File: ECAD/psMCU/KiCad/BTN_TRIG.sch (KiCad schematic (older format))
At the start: 9 parts, among them SW4 Btn, U284 SN74LVC1G17DCK, U285 SN74LVC1G32DCK

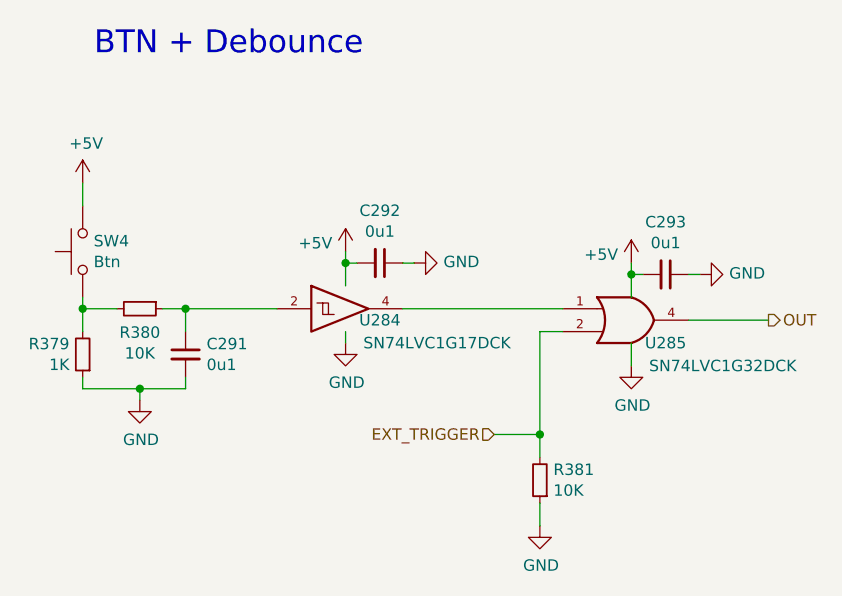
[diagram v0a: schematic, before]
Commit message: Sch: Fixed SYS1 Register
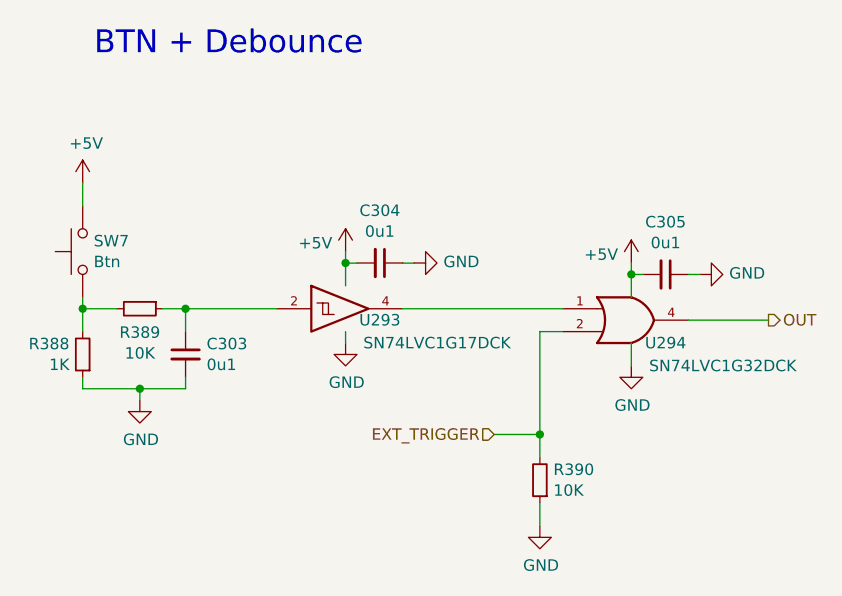
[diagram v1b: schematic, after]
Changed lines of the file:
@@
 $Descr A4 11693 8268
 encoding utf-8
-Sheet 73 97
+Sheet 76 97
 Title "psMCU"
 Date "2022-02-13"
@@
 AR Path="/5FD4EE20/5FF9246F/5FEC0A8B" Ref="C309"  Part="1"
 AR Path="/5FD4EE20/5FF933B5/5FEC0A8B" Ref="C312"  Part="1"
-F 0 "C291" H 4792 3546 50  0000 L CNN
+F 0 "C303" H 4792 3546 50  0000 L CNN
 F 1 "0u1" H 4792 3455 50  0000 L CNN
 F 2 "NoRef_Footprints:C_0603_1608Metric_NoRef" H 4700 3500 50  0001 C CNN
@@
 AR Path="/5FD4EE20/5FF9246F/5FEC0A91" Ref="R395"  Part="1"
 AR Path="/5FD4EE20/5FF933B5/5FEC0A91" Ref="R398"  Part="1"
-F 0 "R380" V 4604 3300 50  0000 C CNN
+F 0 "R389" V 4604 3300 50  0000 C CNN
 F 1 "10K" V 4695 3300 50  0000 C CNN
 F 2 "NoRef_Footprints:R_0603_1608Metric_NoRef" H 4500 3300 50  0001 C CNN
@@
 AR Path="/5FD4EE20/5FF9246F/5FEC0A97" Ref="R44"  Part="1"
 AR Path="/5FD4EE20/5FF933B5/5FEC0A97" Ref="R397"  Part="1"
-F 0 "R379" H 4308 3454 50  0000 L CNN
+F 0 "R388" H 4308 3454 50  0000 L CNN
 F 1 "1K" H 4308 3545 50  0000 L CNN
 F 2 "NoRef_Footprints:R_0603_1608Metric_NoRef" H 4250 3500 50  0001 C CNN
@@
 AR Path="/5FD4EE20/5FF9246F/5FEC0AA6" Ref="#PWR01314"  Part="1"
 AR Path="/5FD4EE20/5FF933B5/5FEC0AA6" Ref="#PWR01323"  Part="1"
-F 0 "#PWR01323" H 4250 2600 50  0001 C CNN
+F 0 "#PWR01296" H 4250 2600 50  0001 C CNN
 F 1 "+5V" H 4265 2923 50  0000 C CNN
 F 2 "" H 4250 2750 50  0001 C CNN
@@
 AR Path="/5FD4EE20/5FF9246F/5FEC0AAC" Ref="#PWR01315"  Part="1"
 AR Path="/5FD4EE20/5FF933B5/5FEC0AAC" Ref="#PWR01324"  Part="1"
-F 0 "#PWR01324" H 4500 3450 50  0001 C CNN
+F 0 "#PWR01297" H 4500 3450 50  0001 C CNN
 F 1 "GND" H 4505 3527 50  0000 C CNN
 F 2 "" H 4500 3700 50  0001 C CNN
@@
 AR Path="/5FD4EE20/5FF9246F/5FFA26E6" Ref="U297"  Part="1"
 AR Path="/5FD4EE20/5FF933B5/5FFA26E6" Ref="U299"  Part="1"
-F 0 "U284" H 5550 3250 50  0000 C CNN
+F 0 "U293" H 5550 3250 50  0000 C CNN
 F 1 "SN74LVC1G17DCK" H 5800 3150 50  0000 C CNN
 F 2 "Package_TO_SOT_SMD:SOT-353_SC-70-5" H 5400 3300 50  0001 C CNN
@@
 AR Path="/5FD4EE20/5FF9246F/5FFA26ED" Ref="#PWR01318"  Part="1"
 AR Path="/5FD4EE20/5FF933B5/5FFA26ED" Ref="#PWR01327"  Part="1"
-F 0 "#PWR01327" H 5700 2850 50  0001 C CNN
+F 0 "#PWR01300" H 5700 2850 50  0001 C CNN
 F 1 "GND" V 5705 2972 50  0000 R CNN
 F 2 "" H 5700 3100 50  0001 C CNN
@@
 AR Path="/5FD4EE20/5FF9246F/5FFA26F6" Ref="C310"  Part="1"
 AR Path="/5FD4EE20/5FF933B5/5FFA26F6" Ref="C313"  Part="1"
-F 0 "C292" V 5321 3100 50  0000 C CNN
+F 0 "C304" V 5321 3100 50  0000 C CNN
 F 1 "0u1" V 5412 3100 50  0000 C CNN
 F 2 "NoRef_Footprints:C_0603_1608Metric_NoRef" H 5550 3100 50  0001 C CNN
@@
 AR Path="/5FD4EE20/5FF9246F/5FFA26FC" Ref="#PWR01316"  Part="1"
 AR Path="/5FD4EE20/5FF933B5/5FFA26FC" Ref="#PWR01325"  Part="1"
-F 0 "#PWR01325" H 5400 2900 50  0001 C CNN
+F 0 "#PWR01298" H 5400 2900 50  0001 C CNN
 F 1 "+5V" H 5342 3087 50  0000 R CNN
 F 2 "" H 5400 3050 50  0001 C CNN
@@
 AR Path="/5FD4EE20/5FF9246F/5FFA2703" Ref="#PWR01317"  Part="1"
 AR Path="/5FD4EE20/5FF933B5/5FFA2703" Ref="#PWR01326"  Part="1"
-F 0 "#PWR01326" H 5400 3200 50  0001 C CNN
+F 0 "#PWR01299" H 5400 3200 50  0001 C CNN
 F 1 "GND" H 5405 3277 50  0000 C CNN
 F 2 "" H 5400 3450 50  0001 C CNN
@@
 AR Path="/5FD4EE20/5FF9246F/6006DFAD" Ref="#PWR01322"  Part="1"
 AR Path="/5FD4EE20/5FF933B5/6006DFAD" Ref="#PWR01331"  Part="1"
-F 0 "#PWR01331" H 6950 2900 50  0001 C CNN
+F 0 "#PWR01304" H 6950 2900 50  0001 C CNN
 F 1 "GND" V 6955 3022 50  0000 R CNN
 F 2 "" H 6950 3150 50  0001 C CNN
@@
 AR Path="/5FD4EE20/5FF9246F/6007A0C4" Ref="R396"  Part="1"
 AR Path="/5FD4EE20/5FF933B5/6007A0C4" Ref="R399"  Part="1"
-F 0 "R381" H 6191 4004 50  0000 R CNN
+F 0 "R390" H 6191 4004 50  0000 R CNN
 F 1 "10K" H 6191 4095 50  0000 R CNN
 F 2 "NoRef_Footprints:R_0603_1608Metric_NoRef" H 6250 4050 50  0001 C CNN
@@
 AR Path="/5FD4EE20/5FF9246F/5FEC0A85" Ref="SW9"  Part="1"
 AR Path="/5FD4EE20/5FF933B5/5FEC0A85" Ref="SW10"  Part="1"
-F 0 "SW4" V 4296 3002 50  0000 R CNN
+F 0 "SW7" V 4296 3002 50  0000 R CNN
 F 1 "Btn" V 4205 3002 50  0000 R CNN
 F 2 "Button_Switch_THT:SW_PUSH_6mm" H 4250 3250 50  0001 C CNN
@@
 AR Path="/5FD4EE20/5FF9246F/6007AB1D" Ref="#PWR01319"  Part="1"
 AR Path="/5FD4EE20/5FF933B5/6007AB1D" Ref="#PWR01328"  Part="1"
-F 0 "#PWR01328" H 6250 4000 50  0001 C CNN
+F 0 "#PWR01301" H 6250 4000 50  0001 C CNN
 F 1 "GND" H 6255 4077 50  0000 C CNN
 F 2 "" H 6250 4250 50  0001 C CNN
@@
 AR Path="/5FD4EE20/5FF9246F/6006DFA4" Ref="C311"  Part="1"
 AR Path="/5FD4EE20/5FF933B5/6006DFA4" Ref="C314"  Part="1"
-F 0 "C293" V 6571 3150 50  0000 C CNN
+F 0 "C305" V 6571 3150 50  0000 C CNN
 F 1 "0u1" V 6662 3150 50  0000 C CNN
 F 2 "NoRef_Footprints:C_0603_1608Metric_NoRef" H 6800 3150 50  0001 C CNN
@@
 AR Path="/5FD4EE20/5FF9246F/6006DF9E" Ref="#PWR01320"  Part="1"
 AR Path="/5FD4EE20/5FF933B5/6006DF9E" Ref="#PWR01329"  Part="1"
-F 0 "#PWR01329" H 6650 2950 50  0001 C CNN
+F 0 "#PWR01302" H 6650 2950 50  0001 C CNN
 F 1 "+5V" H 6592 3137 50  0000 R CNN
 F 2 "" H 6650 3100 50  0001 C CNN
@@
 AR Path="/5FD4EE20/5FF9246F/6006DF96" Ref="#PWR01321"  Part="1"
 AR Path="/5FD4EE20/5FF933B5/6006DF96" Ref="#PWR01330"  Part="1"
-F 0 "#PWR01330" H 6650 3300 50  0001 C CNN
+F 0 "#PWR01303" H 6650 3300 50  0001 C CNN
 F 1 "GND" H 6655 3377 50  0000 C CNN
 F 2 "" H 6650 3550 50  0001 C CNN
@@
 AR Path="/5FD4EE20/5FF9246F/6006DF90" Ref="U298"  Part="1"
 AR Path="/5FD4EE20/5FF933B5/6006DF90" Ref="U300"  Part="1"
-F 0 "U285" H 6800 3250 50  0000 C CNN
+F 0 "U294" H 6800 3250 50  0000 C CNN
 F 1 "SN74LVC1G32DCK" H 7050 3150 50  0000 C CNN
 F 2 "Package_TO_SOT_SMD:SOT-353_SC-70-5" H 6650 3350 50  0001 C CNN

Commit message: Sch: Changed LDD behaviour (now is literal+b)
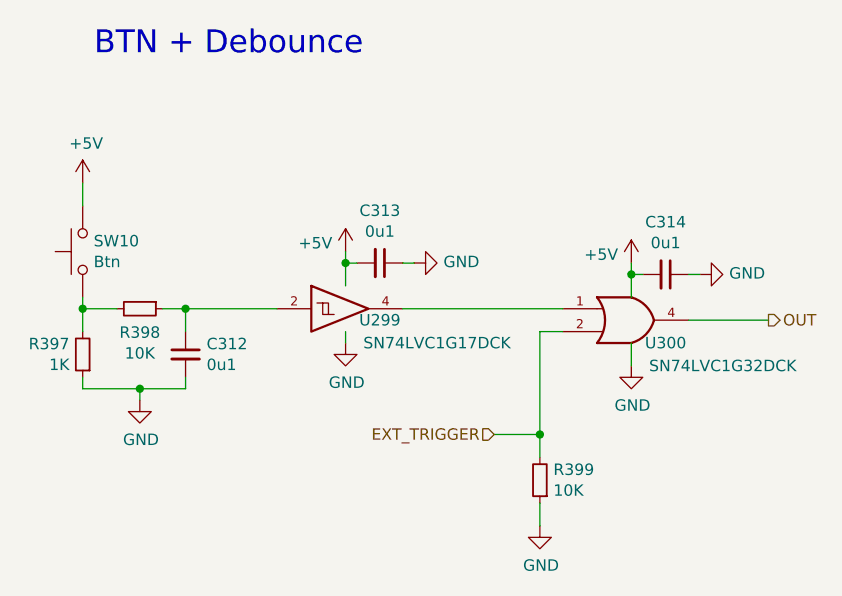
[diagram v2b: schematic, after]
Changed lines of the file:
@@
 $Descr A4 11693 8268
 encoding utf-8
-Sheet 76 97
+Sheet 79 97
 Title "psMCU"
 Date "2022-02-13"
@@
 AR Path="/5FD4EE20/5FF9246F/5FEC0A8B" Ref="C309"  Part="1"
 AR Path="/5FD4EE20/5FF933B5/5FEC0A8B" Ref="C312"  Part="1"
-F 0 "C303" H 4792 3546 50  0000 L CNN
+F 0 "C312" H 4792 3546 50  0000 L CNN
 F 1 "0u1" H 4792 3455 50  0000 L CNN
 F 2 "NoRef_Footprints:C_0603_1608Metric_NoRef" H 4700 3500 50  0001 C CNN
@@
 AR Path="/5FD4EE20/5FF9246F/5FEC0A91" Ref="R395"  Part="1"
 AR Path="/5FD4EE20/5FF933B5/5FEC0A91" Ref="R398"  Part="1"
-F 0 "R389" V 4604 3300 50  0000 C CNN
+F 0 "R398" V 4604 3300 50  0000 C CNN
 F 1 "10K" V 4695 3300 50  0000 C CNN
 F 2 "NoRef_Footprints:R_0603_1608Metric_NoRef" H 4500 3300 50  0001 C CNN
@@
 AR Path="/5FD4EE20/5FF9246F/5FEC0A97" Ref="R44"  Part="1"
 AR Path="/5FD4EE20/5FF933B5/5FEC0A97" Ref="R397"  Part="1"
-F 0 "R388" H 4308 3454 50  0000 L CNN
+F 0 "R397" H 4308 3454 50  0000 L CNN
 F 1 "1K" H 4308 3545 50  0000 L CNN
 F 2 "NoRef_Footprints:R_0603_1608Metric_NoRef" H 4250 3500 50  0001 C CNN
@@
 AR Path="/5FD4EE20/5FF9246F/5FEC0AA6" Ref="#PWR01314"  Part="1"
 AR Path="/5FD4EE20/5FF933B5/5FEC0AA6" Ref="#PWR01323"  Part="1"
-F 0 "#PWR01296" H 4250 2600 50  0001 C CNN
+F 0 "#PWR01323" H 4250 2600 50  0001 C CNN
 F 1 "+5V" H 4265 2923 50  0000 C CNN
 F 2 "" H 4250 2750 50  0001 C CNN
@@
 AR Path="/5FD4EE20/5FF9246F/5FEC0AAC" Ref="#PWR01315"  Part="1"
 AR Path="/5FD4EE20/5FF933B5/5FEC0AAC" Ref="#PWR01324"  Part="1"
-F 0 "#PWR01297" H 4500 3450 50  0001 C CNN
+F 0 "#PWR01324" H 4500 3450 50  0001 C CNN
 F 1 "GND" H 4505 3527 50  0000 C CNN
 F 2 "" H 4500 3700 50  0001 C CNN
@@
 AR Path="/5FD4EE20/5FF9246F/5FFA26E6" Ref="U297"  Part="1"
 AR Path="/5FD4EE20/5FF933B5/5FFA26E6" Ref="U299"  Part="1"
-F 0 "U293" H 5550 3250 50  0000 C CNN
+F 0 "U299" H 5550 3250 50  0000 C CNN
 F 1 "SN74LVC1G17DCK" H 5800 3150 50  0000 C CNN
 F 2 "Package_TO_SOT_SMD:SOT-353_SC-70-5" H 5400 3300 50  0001 C CNN
@@
 AR Path="/5FD4EE20/5FF9246F/5FFA26ED" Ref="#PWR01318"  Part="1"
 AR Path="/5FD4EE20/5FF933B5/5FFA26ED" Ref="#PWR01327"  Part="1"
-F 0 "#PWR01300" H 5700 2850 50  0001 C CNN
+F 0 "#PWR01327" H 5700 2850 50  0001 C CNN
 F 1 "GND" V 5705 2972 50  0000 R CNN
 F 2 "" H 5700 3100 50  0001 C CNN
@@
 AR Path="/5FD4EE20/5FF9246F/5FFA26F6" Ref="C310"  Part="1"
 AR Path="/5FD4EE20/5FF933B5/5FFA26F6" Ref="C313"  Part="1"
-F 0 "C304" V 5321 3100 50  0000 C CNN
+F 0 "C313" V 5321 3100 50  0000 C CNN
 F 1 "0u1" V 5412 3100 50  0000 C CNN
 F 2 "NoRef_Footprints:C_0603_1608Metric_NoRef" H 5550 3100 50  0001 C CNN
@@
 AR Path="/5FD4EE20/5FF9246F/5FFA26FC" Ref="#PWR01316"  Part="1"
 AR Path="/5FD4EE20/5FF933B5/5FFA26FC" Ref="#PWR01325"  Part="1"
-F 0 "#PWR01298" H 5400 2900 50  0001 C CNN
+F 0 "#PWR01325" H 5400 2900 50  0001 C CNN
 F 1 "+5V" H 5342 3087 50  0000 R CNN
 F 2 "" H 5400 3050 50  0001 C CNN
@@
 AR Path="/5FD4EE20/5FF9246F/5FFA2703" Ref="#PWR01317"  Part="1"
 AR Path="/5FD4EE20/5FF933B5/5FFA2703" Ref="#PWR01326"  Part="1"
-F 0 "#PWR01299" H 5400 3200 50  0001 C CNN
+F 0 "#PWR01326" H 5400 3200 50  0001 C CNN
 F 1 "GND" H 5405 3277 50  0000 C CNN
 F 2 "" H 5400 3450 50  0001 C CNN
@@
 AR Path="/5FD4EE20/5FF9246F/6006DFAD" Ref="#PWR01322"  Part="1"
 AR Path="/5FD4EE20/5FF933B5/6006DFAD" Ref="#PWR01331"  Part="1"
-F 0 "#PWR01304" H 6950 2900 50  0001 C CNN
+F 0 "#PWR01331" H 6950 2900 50  0001 C CNN
 F 1 "GND" V 6955 3022 50  0000 R CNN
 F 2 "" H 6950 3150 50  0001 C CNN
@@
 AR Path="/5FD4EE20/5FF9246F/6007A0C4" Ref="R396"  Part="1"
 AR Path="/5FD4EE20/5FF933B5/6007A0C4" Ref="R399"  Part="1"
-F 0 "R390" H 6191 4004 50  0000 R CNN
+F 0 "R399" H 6191 4004 50  0000 R CNN
 F 1 "10K" H 6191 4095 50  0000 R CNN
 F 2 "NoRef_Footprints:R_0603_1608Metric_NoRef" H 6250 4050 50  0001 C CNN
@@
 AR Path="/5FD4EE20/5FF9246F/5FEC0A85" Ref="SW9"  Part="1"
 AR Path="/5FD4EE20/5FF933B5/5FEC0A85" Ref="SW10"  Part="1"
-F 0 "SW7" V 4296 3002 50  0000 R CNN
+F 0 "SW10" V 4296 3002 50  0000 R CNN
 F 1 "Btn" V 4205 3002 50  0000 R CNN
 F 2 "Button_Switch_THT:SW_PUSH_6mm" H 4250 3250 50  0001 C CNN
@@
 AR Path="/5FD4EE20/5FF9246F/6007AB1D" Ref="#PWR01319"  Part="1"
 AR Path="/5FD4EE20/5FF933B5/6007AB1D" Ref="#PWR01328"  Part="1"
-F 0 "#PWR01301" H 6250 4000 50  0001 C CNN
+F 0 "#PWR01328" H 6250 4000 50  0001 C CNN
 F 1 "GND" H 6255 4077 50  0000 C CNN
 F 2 "" H 6250 4250 50  0001 C CNN
@@
 AR Path="/5FD4EE20/5FF9246F/6006DFA4" Ref="C311"  Part="1"
 AR Path="/5FD4EE20/5FF933B5/6006DFA4" Ref="C314"  Part="1"
-F 0 "C305" V 6571 3150 50  0000 C CNN
+F 0 "C314" V 6571 3150 50  0000 C CNN
 F 1 "0u1" V 6662 3150 50  0000 C CNN
 F 2 "NoRef_Footprints:C_0603_1608Metric_NoRef" H 6800 3150 50  0001 C CNN
@@
 AR Path="/5FD4EE20/5FF9246F/6006DF9E" Ref="#PWR01320"  Part="1"
 AR Path="/5FD4EE20/5FF933B5/6006DF9E" Ref="#PWR01329"  Part="1"
-F 0 "#PWR01302" H 6650 2950 50  0001 C CNN
+F 0 "#PWR01329" H 6650 2950 50  0001 C CNN
 F 1 "+5V" H 6592 3137 50  0000 R CNN
 F 2 "" H 6650 3100 50  0001 C CNN
@@
 AR Path="/5FD4EE20/5FF9246F/6006DF96" Ref="#PWR01321"  Part="1"
 AR Path="/5FD4EE20/5FF933B5/6006DF96" Ref="#PWR01330"  Part="1"
-F 0 "#PWR01303" H 6650 3300 50  0001 C CNN
+F 0 "#PWR01330" H 6650 3300 50  0001 C CNN
 F 1 "GND" H 6655 3377 50  0000 C CNN
 F 2 "" H 6650 3550 50  0001 C CNN
@@
 AR Path="/5FD4EE20/5FF9246F/6006DF90" Ref="U298"  Part="1"
 AR Path="/5FD4EE20/5FF933B5/6006DF90" Ref="U300"  Part="1"
-F 0 "U294" H 6800 3250 50  0000 C CNN
+F 0 "U300" H 6800 3250 50  0000 C CNN
 F 1 "SN74LVC1G32DCK" H 7050 3150 50  0000 C CNN
 F 2 "Package_TO_SOT_SMD:SOT-353_SC-70-5" H 6650 3350 50  0001 C CNN

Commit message: Sch: Cleanup + Small fixes
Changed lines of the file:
@@
 $Descr A4 11693 8268
 encoding utf-8
-Sheet 75 109
+Sheet 88 109
 Title "psMCU"
 Date "2022-02-13"
@@
 AR Path="/5FD4EE20/5FF9246F/5FEC0A8B" Ref="C309"  Part="1"
 AR Path="/5FD4EE20/5FF933B5/5FEC0A8B" Ref="C312"  Part="1"
-F 0 "C312" H 4792 3546 50  0000 L CNN
+F 0 "C291" H 4792 3546 50  0000 L CNN
 F 1 "0u1" H 4792 3455 50  0000 L CNN
 F 2 "NoRef_Footprints:C_0603_1608Metric_NoRef" H 4700 3500 50  0001 C CNN
@@
 AR Path="/5FD4EE20/5FF9246F/5FEC0A91" Ref="R395"  Part="1"
 AR Path="/5FD4EE20/5FF933B5/5FEC0A91" Ref="R398"  Part="1"
-F 0 "R398" V 4604 3300 50  0000 C CNN
+F 0 "R380" V 4604 3300 50  0000 C CNN
 F 1 "10K" V 4695 3300 50  0000 C CNN
 F 2 "NoRef_Footprints:R_0603_1608Metric_NoRef" H 4500 3300 50  0001 C CNN
@@
 AR Path="/5FD4EE20/5FF9246F/5FEC0A97" Ref="R44"  Part="1"
 AR Path="/5FD4EE20/5FF933B5/5FEC0A97" Ref="R397"  Part="1"
-F 0 "R397" H 4308 3454 50  0000 L CNN
+F 0 "R379" H 4308 3454 50  0000 L CNN
 F 1 "1K" H 4308 3545 50  0000 L CNN
 F 2 "NoRef_Footprints:R_0603_1608Metric_NoRef" H 4250 3500 50  0001 C CNN
@@
 AR Path="/5FD4EE20/5FF9246F/5FFA26E6" Ref="U297"  Part="1"
 AR Path="/5FD4EE20/5FF933B5/5FFA26E6" Ref="U299"  Part="1"
-F 0 "U299" H 5550 3250 50  0000 C CNN
+F 0 "U284" H 5550 3250 50  0000 C CNN
 F 1 "SN74LVC1G17DCK" H 5800 3150 50  0000 C CNN
 F 2 "Package_TO_SOT_SMD:SOT-353_SC-70-5" H 5400 3300 50  0001 C CNN
@@
 AR Path="/5FD4EE20/5FF9246F/5FFA26F6" Ref="C310"  Part="1"
 AR Path="/5FD4EE20/5FF933B5/5FFA26F6" Ref="C313"  Part="1"
-F 0 "C313" V 5321 3100 50  0000 C CNN
+F 0 "C292" V 5321 3100 50  0000 C CNN
 F 1 "0u1" V 5412 3100 50  0000 C CNN
 F 2 "NoRef_Footprints:C_0603_1608Metric_NoRef" H 5550 3100 50  0001 C CNN
@@
 AR Path="/5FD4EE20/5FF9246F/6007A0C4" Ref="R396"  Part="1"
 AR Path="/5FD4EE20/5FF933B5/6007A0C4" Ref="R399"  Part="1"
-F 0 "R399" H 6191 4004 50  0000 R CNN
+F 0 "R381" H 6191 4004 50  0000 R CNN
 F 1 "10K" H 6191 4095 50  0000 R CNN
 F 2 "NoRef_Footprints:R_0603_1608Metric_NoRef" H 6250 4050 50  0001 C CNN
@@
 AR Path="/5FD4EE20/5FF9246F/5FEC0A85" Ref="SW9"  Part="1"
 AR Path="/5FD4EE20/5FF933B5/5FEC0A85" Ref="SW10"  Part="1"
-F 0 "SW10" V 4296 3002 50  0000 R CNN
+F 0 "SW4" V 4296 3002 50  0000 R CNN
 F 1 "Btn" V 4205 3002 50  0000 R CNN
 F 2 "Button_Switch_THT:SW_PUSH_6mm" H 4250 3250 50  0001 C CNN
@@
 AR Path="/5FD4EE20/5FF9246F/6006DFA4" Ref="C311"  Part="1"
 AR Path="/5FD4EE20/5FF933B5/6006DFA4" Ref="C314"  Part="1"
-F 0 "C314" V 6571 3150 50  0000 C CNN
+F 0 "C293" V 6571 3150 50  0000 C CNN
 F 1 "0u1" V 6662 3150 50  0000 C CNN
 F 2 "NoRef_Footprints:C_0603_1608Metric_NoRef" H 6800 3150 50  0001 C CNN
@@
 AR Path="/5FD4EE20/5FF9246F/6006DF90" Ref="U298"  Part="1"
 AR Path="/5FD4EE20/5FF933B5/6006DF90" Ref="U300"  Part="1"
-F 0 "U300" H 6800 3250 50  0000 C CNN
+F 0 "U285" H 6800 3250 50  0000 C CNN
 F 1 "SN74LVC1G32DCK" H 7050 3150 50  0000 C CNN
 F 2 "Package_TO_SOT_SMD:SOT-353_SC-70-5" H 6650 3350 50  0001 C CNN
